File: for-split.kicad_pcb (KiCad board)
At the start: 2 copper layers, 114.3 x 95.3 mm, 75 parts, among them J1 TRRS, J2 TRRS, U1 ProMicro

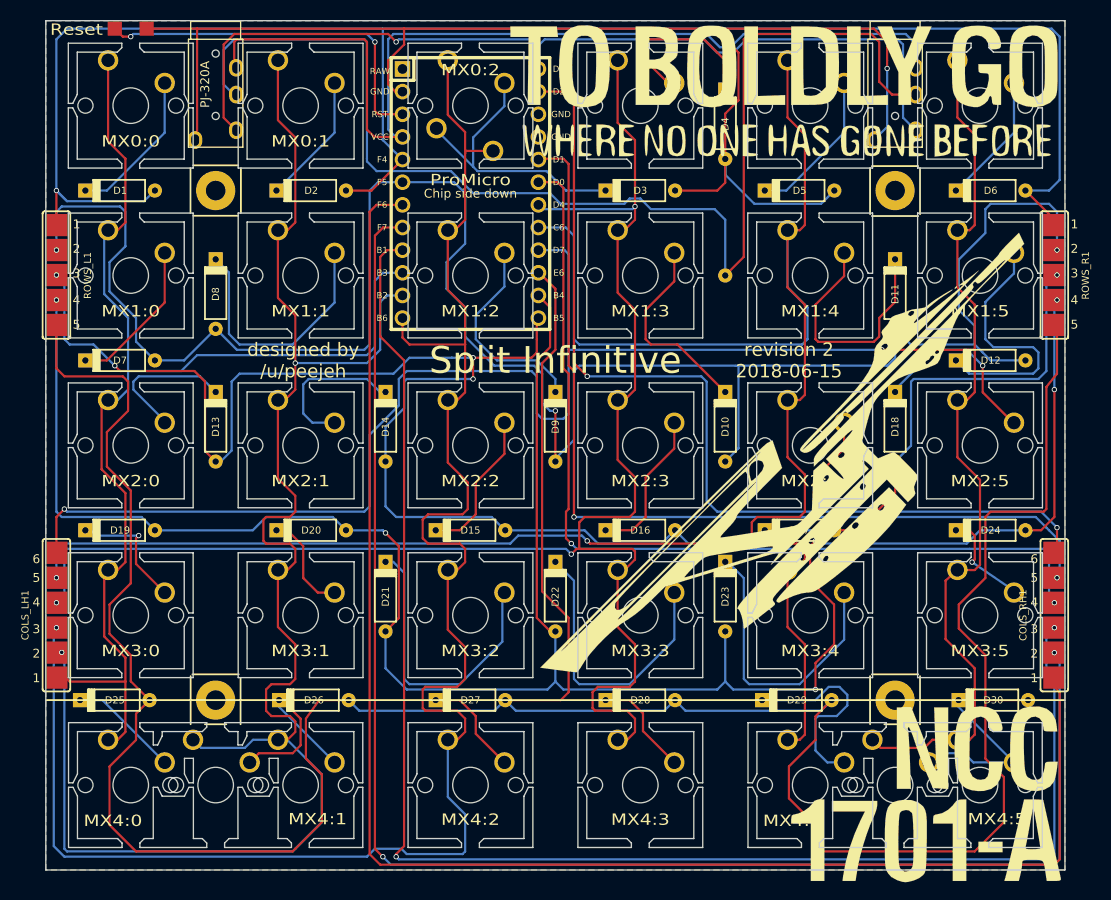
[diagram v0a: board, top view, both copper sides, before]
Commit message: chore: removed 2U switches and edge connections, missing traces on switches because I think nets are munged
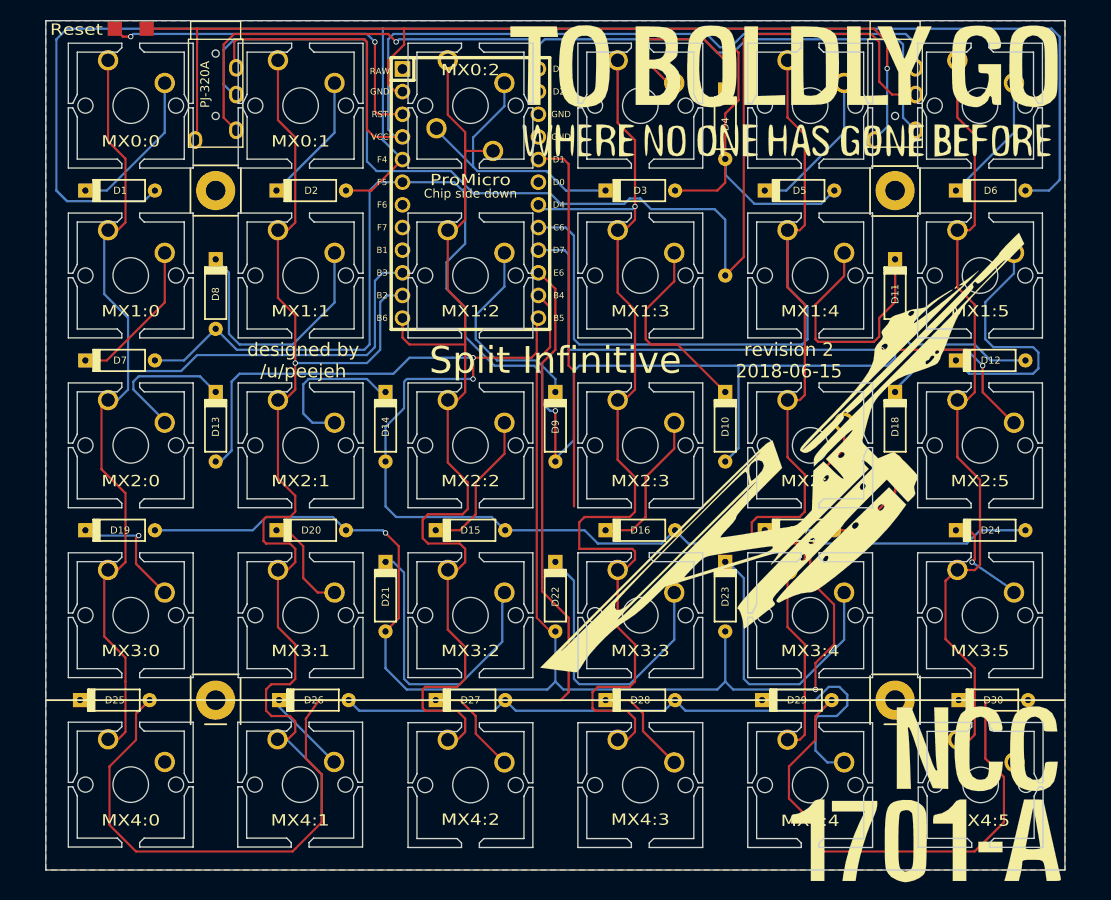
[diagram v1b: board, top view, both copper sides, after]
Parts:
- removed COLS_LH1, COLS_RH1: Conn_01x06, idle-hands:CONNECTOR_6
- removed ROWS_L1, ROWS_R1: Conn_01x05, idle-hands:CONNECTOR_5
- MX4:0: footprint idle-hands:MX -> idle-hands:MX_CUTOUT
- MX4:1: footprint idle-hands:MX2U_CUTOUT -> idle-hands:MX_CUTOUT
- MX4:4: value MX4:7 -> MX3:7; footprint idle-hands:MX -> idle-hands:MX_CUTOUT
- MX4:5: value MX4:6 -> MX3:7; footprint idle-hands:MX2U_CUTOUT -> idle-hands:MX_CUTOUT
- moved MX4:5 9.59 mm to (212.0, 150.0)
- moved MX4:1 9.47 mm to (135.7, 150.0)
- moved MX4:0 0.05 mm to (116.7, 150.0)
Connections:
- MX4:0 pad 2: Net-(D25-Pad1) -> Net-(D19-Pad1)
- MX4:1 pad 1: /Col1 -> /Col0
- MX4:1 pad 2: Net-(D26-Pad1) -> Net-(D19-Pad1)
- MX4:4 pad 2: Net-(D29-Pad1) -> Net-(D23-Pad1)
- MX4:5 pad 1: /Col5 -> /Col4
- MX4:5 pad 2: Net-(D30-Pad1) -> Net-(D23-Pad1)
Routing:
- net /Col6: track 174.8 -> 0.00 mm
- net /Col7: track 173.4 -> 0.00 mm, vias 2 -> 0
- net /Col8: track 172.1 -> 0.00 mm, vias 2 -> 0
- net /Col11: track 106.2 -> 0.00 mm, vias 2 -> 0
- net /Row4: track 342.2 -> 236.7 mm
- net /Col9: track 103.3 -> 0.00 mm, vias 2 -> 0
- net /Col5: track 245.4 -> 148.1 mm, vias 2 -> 1
- net /Col2: track 199.9 -> 114.6 mm, vias 1 -> 0
- net /Col4: track 234.5 -> 151.7 mm, vias 2 -> 0
- net /Row2: track 212.0 -> 140.6 mm, vias 5 -> 2
- net /Col3: track 182.4 -> 117.9 mm, vias 3 -> 1
- net /Row3: track 252.7 -> 188.8 mm, vias 6 -> 3
- net /Col1: track 189.2 -> 126.4 mm, vias 2 -> 1
- net /Row1: track 235.1 -> 173.0 mm, vias 3 -> 1
- net /Col10: track 103.4 -> 42.3 mm, vias 2 -> 0
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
